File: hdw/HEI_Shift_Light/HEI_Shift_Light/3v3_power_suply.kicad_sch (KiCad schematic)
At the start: 17 parts

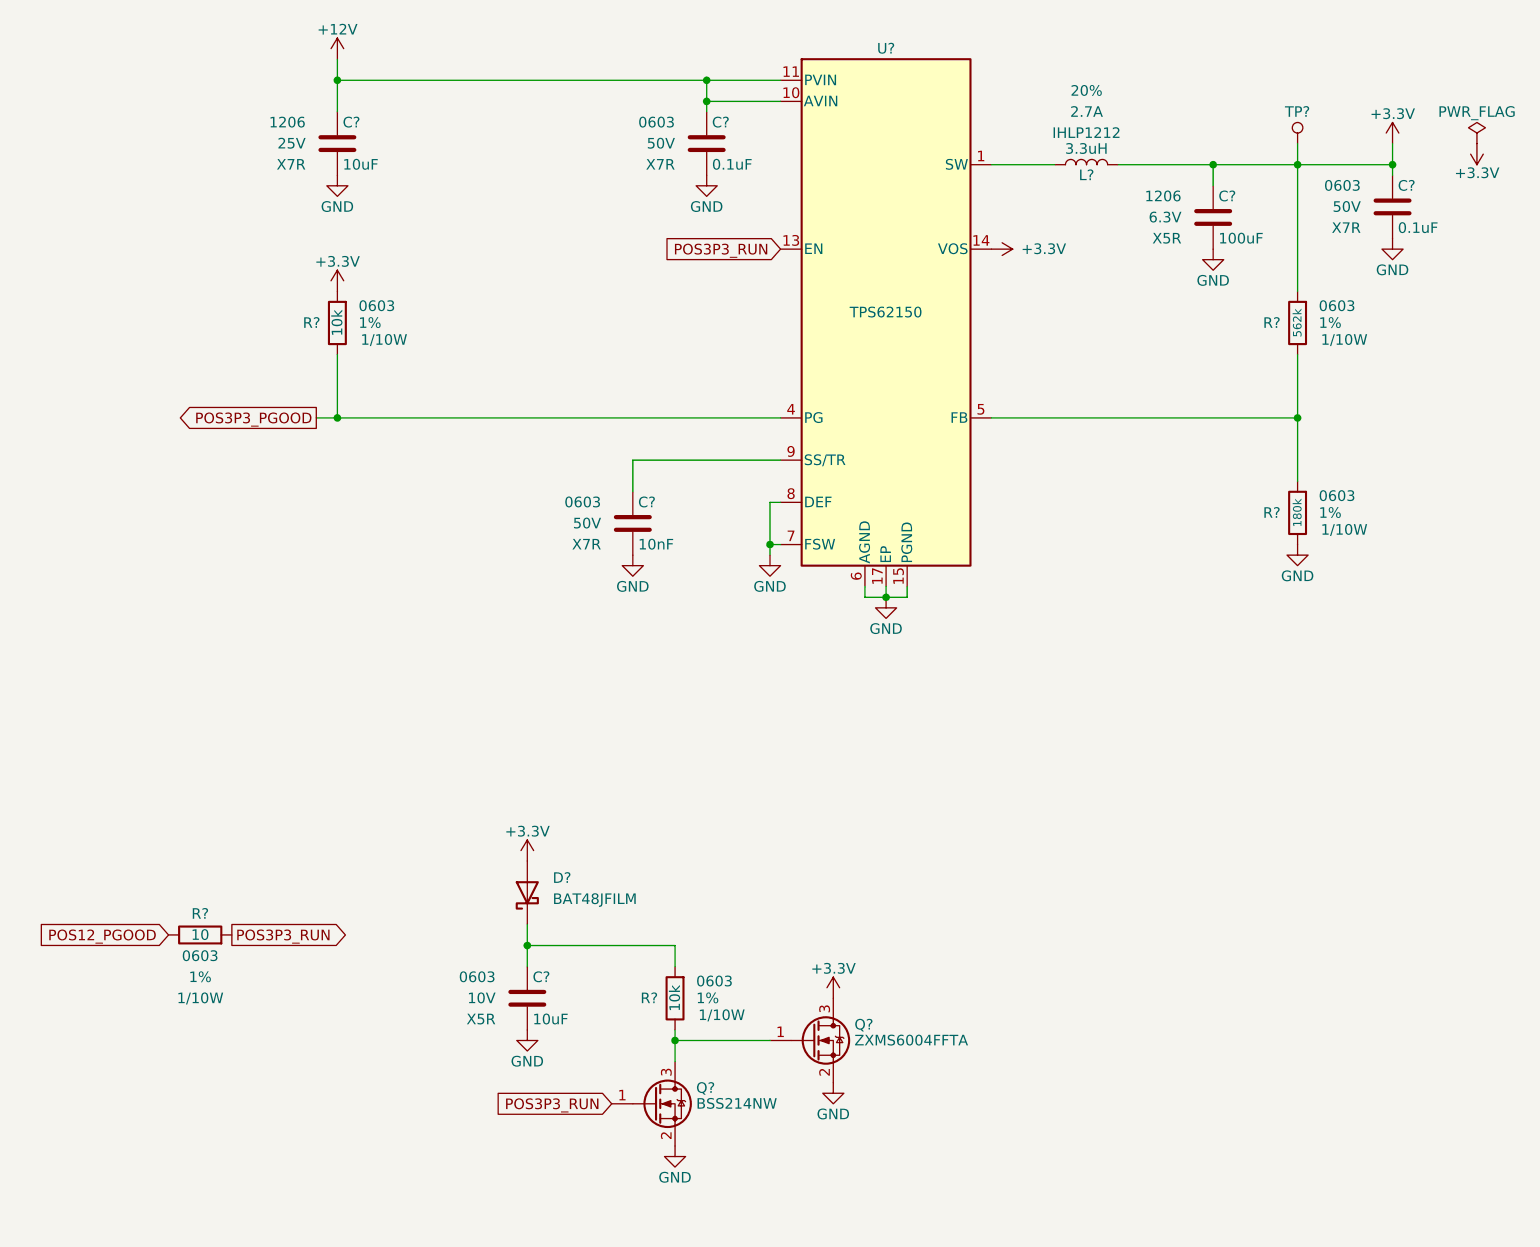
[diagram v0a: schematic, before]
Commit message: Added input power filtering
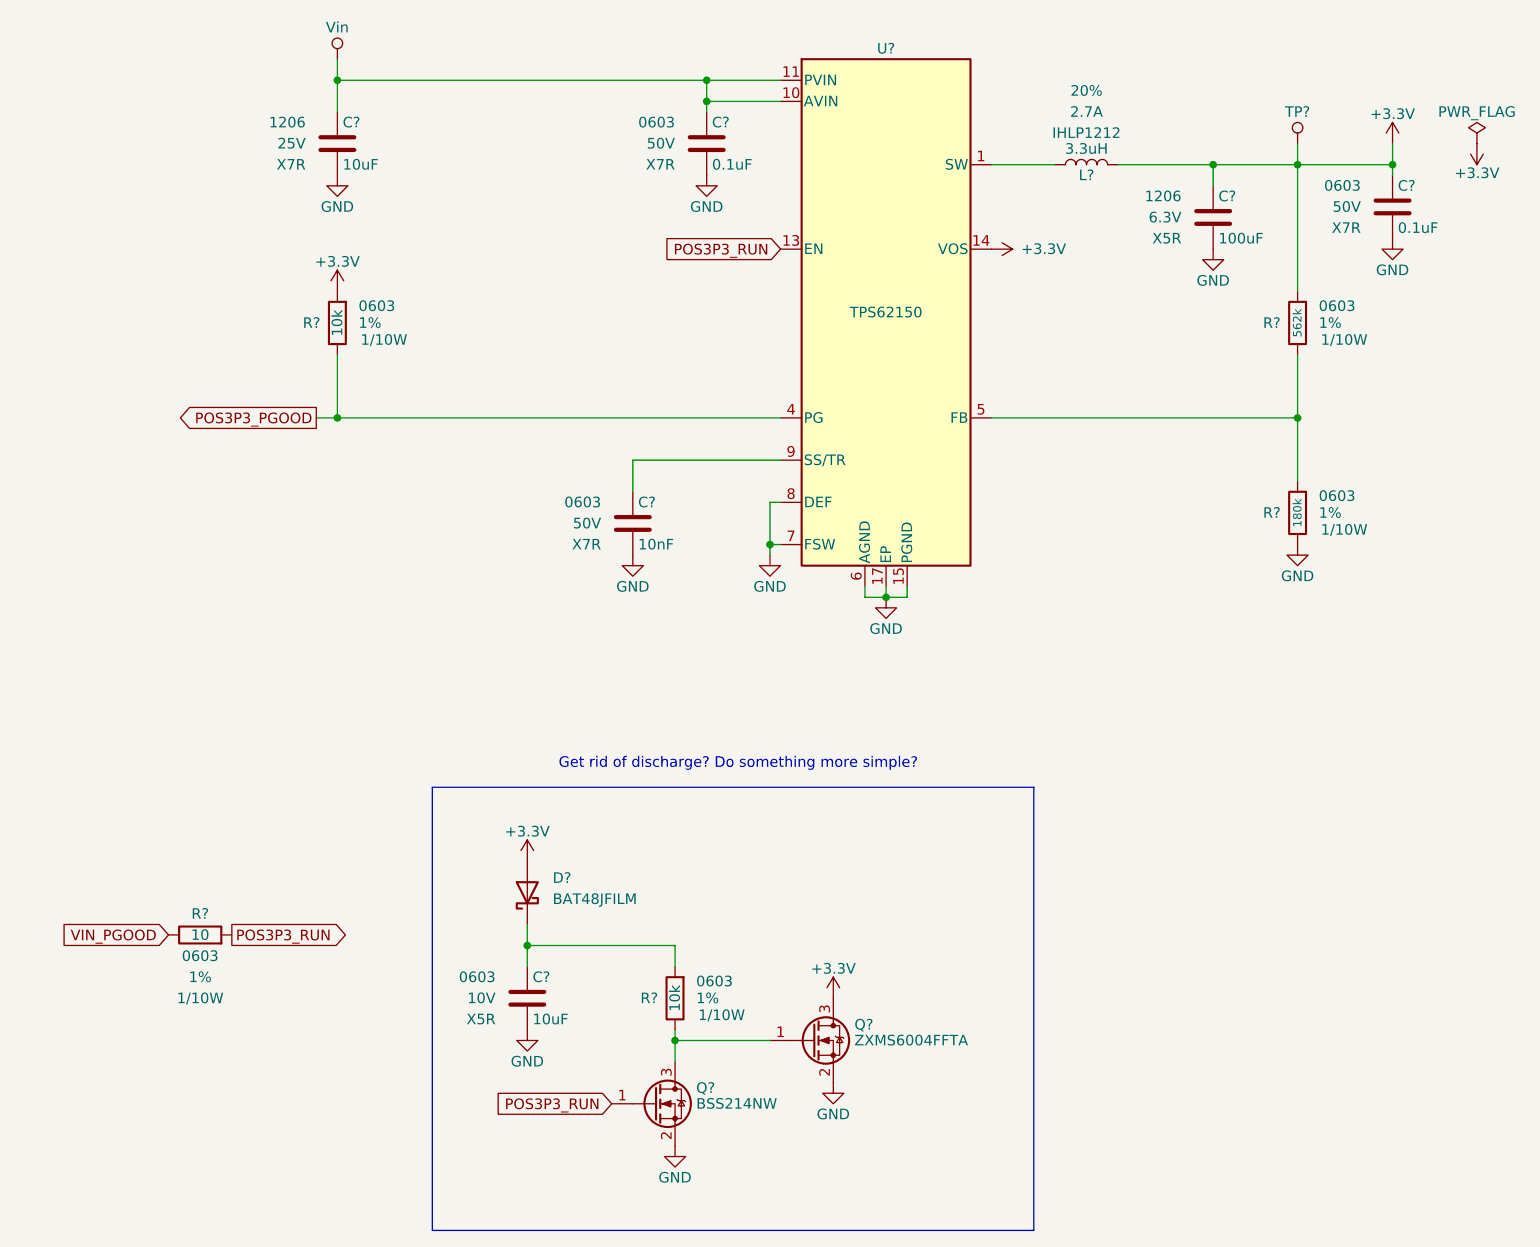
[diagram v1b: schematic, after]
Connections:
- net +12V renamed Vin
- net POS12_PGOOD renamed VIN_PGOOD
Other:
- note added: "Get rid of discharge? Do something more simple?"
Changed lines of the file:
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@@
 	(generator_version "10.0")
 	(paper "A")
+	(rectangle
+		(start 69.85 142.24)
+		(end 142.24 195.58)
+		(stroke
+			(width 0)
+			(type solid)
+			(color 0 0 72 1)
+		)
+		(fill
+			(type hatch)
+			(color 0 0 255 1)
+		)
+	)
+	(text "Get rid of discharge? Do something more simple?"
+		(exclude_from_sim no)
+		(at 106.68 139.446 0)
+		(effects
+			(font
+				(size 1.27 1.27)
+			)
+		)
+	)
 	(junction
 		(at 81.28 161.29)
@@
 		)
 	)
-	(global_label "POS12_PGOOD"
+	(global_label "VIN_PGOOD"
 		(shape input)
 		(at 38.1 160.02 180)
@@
 	)
 	(symbol
-		(lib_id "power:+12V")
-		(at 58.42 54.61 0)
-		(unit 1)
-		(body_style 1)
-		(exclude_from_sim no)
-		(in_bom yes)
-		(on_board yes)
-		(in_pos_files yes)
-		(dnp no)
-		(property "Reference" "#PWR?"
-			(at 58.42 58.42 0)
-			(hide yes)
-			(show_name no)
-			(do_not_autoplace no)
-			(effects
-				(font
-					(size 1.27 1.27)
-				)
-			)
-		)
-		(property "Value" "+12V"
-			(at 58.42 51.054 0)
-			(show_name no)
-			(do_not_autoplace no)
-			(effects
-				(font
-					(size 1.27 1.27)
-				)
-			)
-		)
-		(property "Footprint" ""
-			(at 58.42 54.61 0)
-			(hide yes)
-			(show_name no)
-			(do_not_autoplace no)
-			(effects
-				(font
-					(size 1.27 1.27)
-				)
-			)
-		)
-		(property "Datasheet" ""
-			(at 58.42 54.61 0)
-			(hide yes)
-			(show_name no)
-			(do_not_autoplace no)
-			(effects
-				(font
-					(size 1.27 1.27)
-				)
-			)
-		)
-		(property "Description" ""
-			(at 58.42 54.61 0)
-			(show_name no)
-			(do_not_autoplace no)
-			(effects
-				(font
-					(size 1.27 1.27)
-				)
-			)
-		)
-		(pin "1"
-		)
-		(instances
-			(project "HEI_Shift_Light"
-				(path "/288c8230-69eb-4ad9-929d-f4630114196f/41605f50-4a5f-4515-812e-3b7b65ea4a04"
-					(reference "#PWR?")
-					(unit 1)
-				)
-			)
-		)
-	)
-	(symbol
 		(lib_id "power:GND")
 		(at 163.83 77.47 0)
@@
 					(unit 1)
 				)
+			)
+		)
+	)
+	(symbol
+		(lib_id "Custom Library:Vin")
+		(at 58.42 54.61 0)
+		(unit 1)
+		(body_style 1)
+		(exclude_from_sim no)
+		(in_bom yes)
+		(on_board yes)
+		(in_pos_files yes)
+		(dnp no)
+		(property "Reference" "#PWR015"
+			(at 58.42 58.42 0)
+			(hide yes)
+			(show_name no)
+			(do_not_autoplace no)
+			(effects
+				(font
+					(size 1.27 1.27)
+				)
+			)
+		)
+		(property "Value" "Vin"
+			(at 58.42 50.8 0)
+			(show_name no)
+			(do_not_autoplace no)
+			(effects
+				(font
+					(size 1.27 1.27)
+				)
+			)
+		)
+		(property "Footprint" ""
+			(at 58.42 54.61 0)
+			(show_name no)
+			(do_not_autoplace no)
+			(effects
+				(font
+					(size 1.27 1.27)
+				)
+			)
+		)
+		(property "Datasheet" ""
+			(at 58.42 54.61 0)
+			(show_name no)
+			(do_not_autoplace no)
+			(effects
+				(font
+					(size 1.27 1.27)
+				)
+			)
+		)
+		(property "Description" ""
+			(at 58.42 54.61 0)
+			(hide yes)
+			(show_name no)
+			(do_not_autoplace no)
+			(effects
+				(font
+					(size 1.27 1.27)
+				)
+			)
+		)
+		(pin "1"
+		)
+		(instances
+			(project "HEI_Shift_Light"
+				(path "/288c8230-69eb-4ad9-929d-f4630114196f/41605f50-4a5f-4515-812e-3b7b65ea4a04"
+					(reference "#PWR015")
+					(unit 1)
+				)
